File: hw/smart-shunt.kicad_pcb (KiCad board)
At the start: 2 copper layers, 50.8 x 37.1 mm, 64 parts, among them J1 Screw_Terminal_01x01, J10 Conn_01x01, J11 Conn_01x01, J2 Screw_Terminal_01x01, J3 Conn_01x02_Pin, J4 Conn_01x02_Pin, J5 Conn_01x03_Socket, J6 Conn_01x02_Pin, J7 UEXT_Slave, J8 UEXT_Slave2, U1 INA228, U2 TPT7721-SO1R, U3 TLV74033PDBVR, U4 TPT72616-SO1R, U6 TLV74130PDBVR

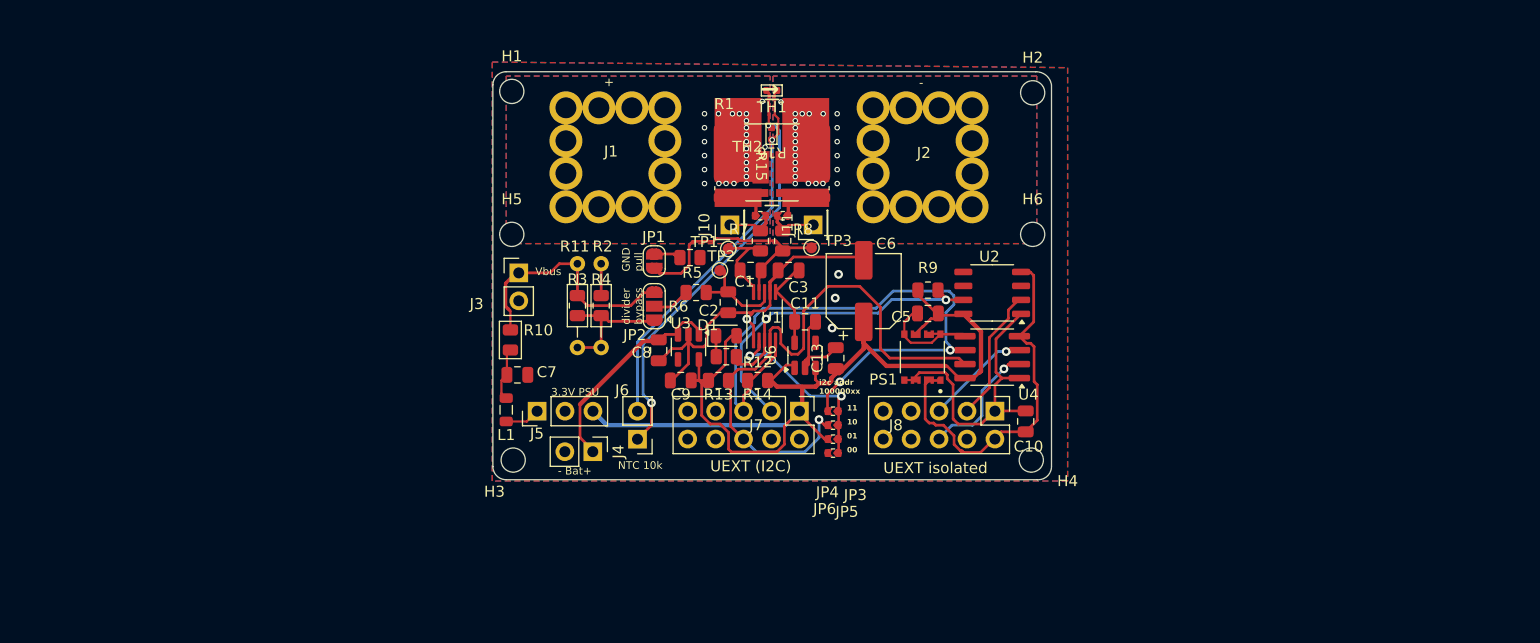
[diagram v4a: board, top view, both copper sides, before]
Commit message: add riedon rsn footprint, copper only path
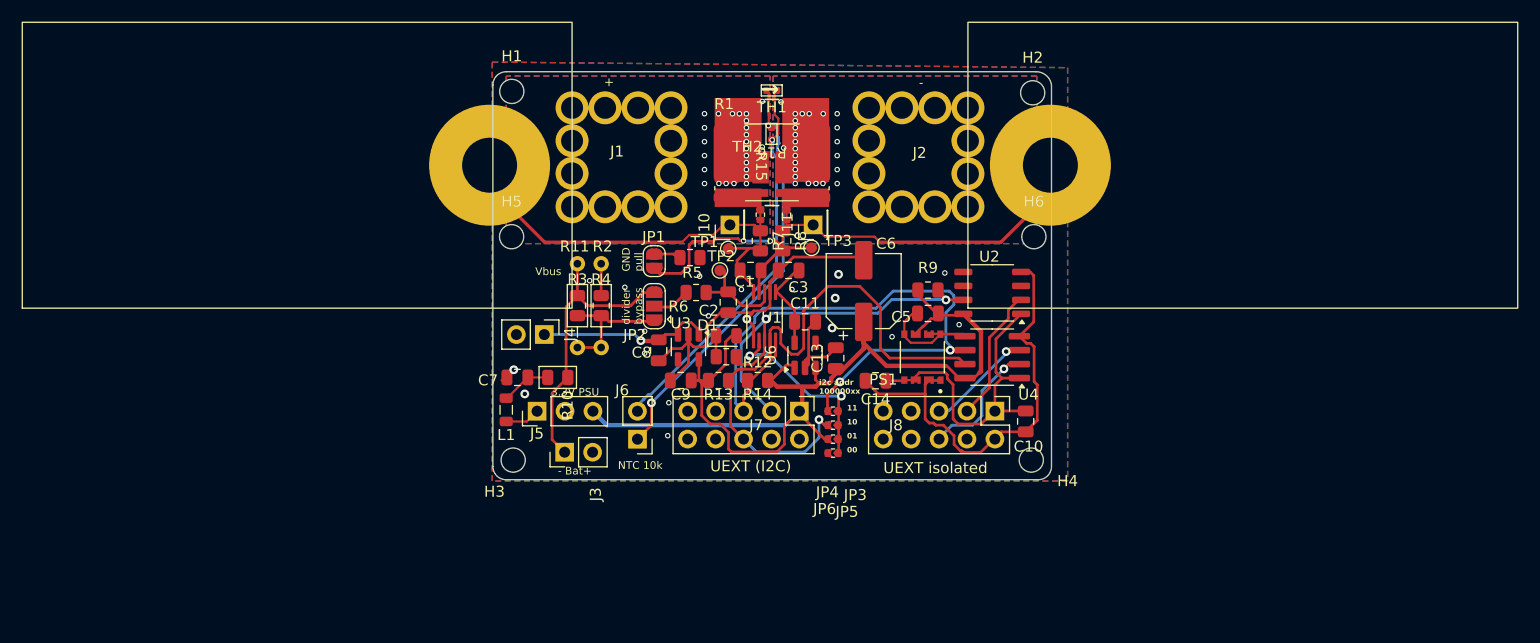
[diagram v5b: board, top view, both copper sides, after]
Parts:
- added C14: 10uF, Capacitor_SMD:C_0805_2012Metric, F.Cu at (113.6, 100.1)
- added J12: Riedon RSN, open-pe:RiedonRSN, B.Cu at (104.0, 80.5)
- JP7, JP8: footprint open-pe:SolderJumper_0402_1005Metric -> open-pe:SolderJumper_0402_1005Metric_Bridged
- R6: value 100 -> 10
- R7, R8: footprint Resistor_SMD:R_0805_2012Metric -> open-pe:R_0805_2012Metric_Bridged
- moved J3 16.8 mm to (85.3, 106.6), turned to 90 degrees
- moved J4 11.5 mm to (83.5, 95.9)
- moved R10 5.49 mm to (84.7, 99.8), turned to 0 degrees
- moved J1 0.56 mm to (92.0, 81.3)
- moved J2 0.38 mm to (119.0, 81.3)
- moved JP8 0.36 mm to (105.5, 85.0), turned to -90 degrees
- moved H6 0.24 mm to (128.0, 87.0)
- moved C7 0.23 mm to (81.0, 99.8), turned to 0 degrees
- moved H5 0.21 mm to (80.5, 87.0)
- moved JP7 0.09 mm to (103.1, 85.0), turned to -90 degrees
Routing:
- net Shunt-: track 4.33 -> 30.5 mm
- net Shunt+: track 4.32 -> 30.0 mm
- net GND2: track 33.9 -> 39.8 mm
- net Vin: track 21.7 -> 25.8 mm
- net Net-(J4-Pin_1): track 20.1 -> 16.3 mm, vias 0 -> 1
- net Net-(JP8-A): track 3.67 -> 0.00 mm
- net Net-(J6-Pin_2): track 38.6 -> 35.3 mm
- net Net-(JP7-A): track 3.64 -> 1.93 mm
- net +3.3V2: track 28.2 -> 29.9 mm
- net GND: track 55.3 -> 55.9 mm, vias 4 -> 19
- net P-: vias 24 -> 25
- net Net-(JP1-B): vias 0 -> 2
